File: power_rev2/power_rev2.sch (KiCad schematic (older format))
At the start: 74 parts, among them J1 Conn_01x02_Female, J2 Conn_01x02_Female, J3 CONN_02X03, J4 Conn_01x06_Female, Q1 BS170, Q11 BS170, Q12 BSB014N04LX3, Q2 BS170, Q3 BS170, Q5 BS170, Q6 BS170, Q7 BS170, U1 MAX1648, U2 TPS2592xx

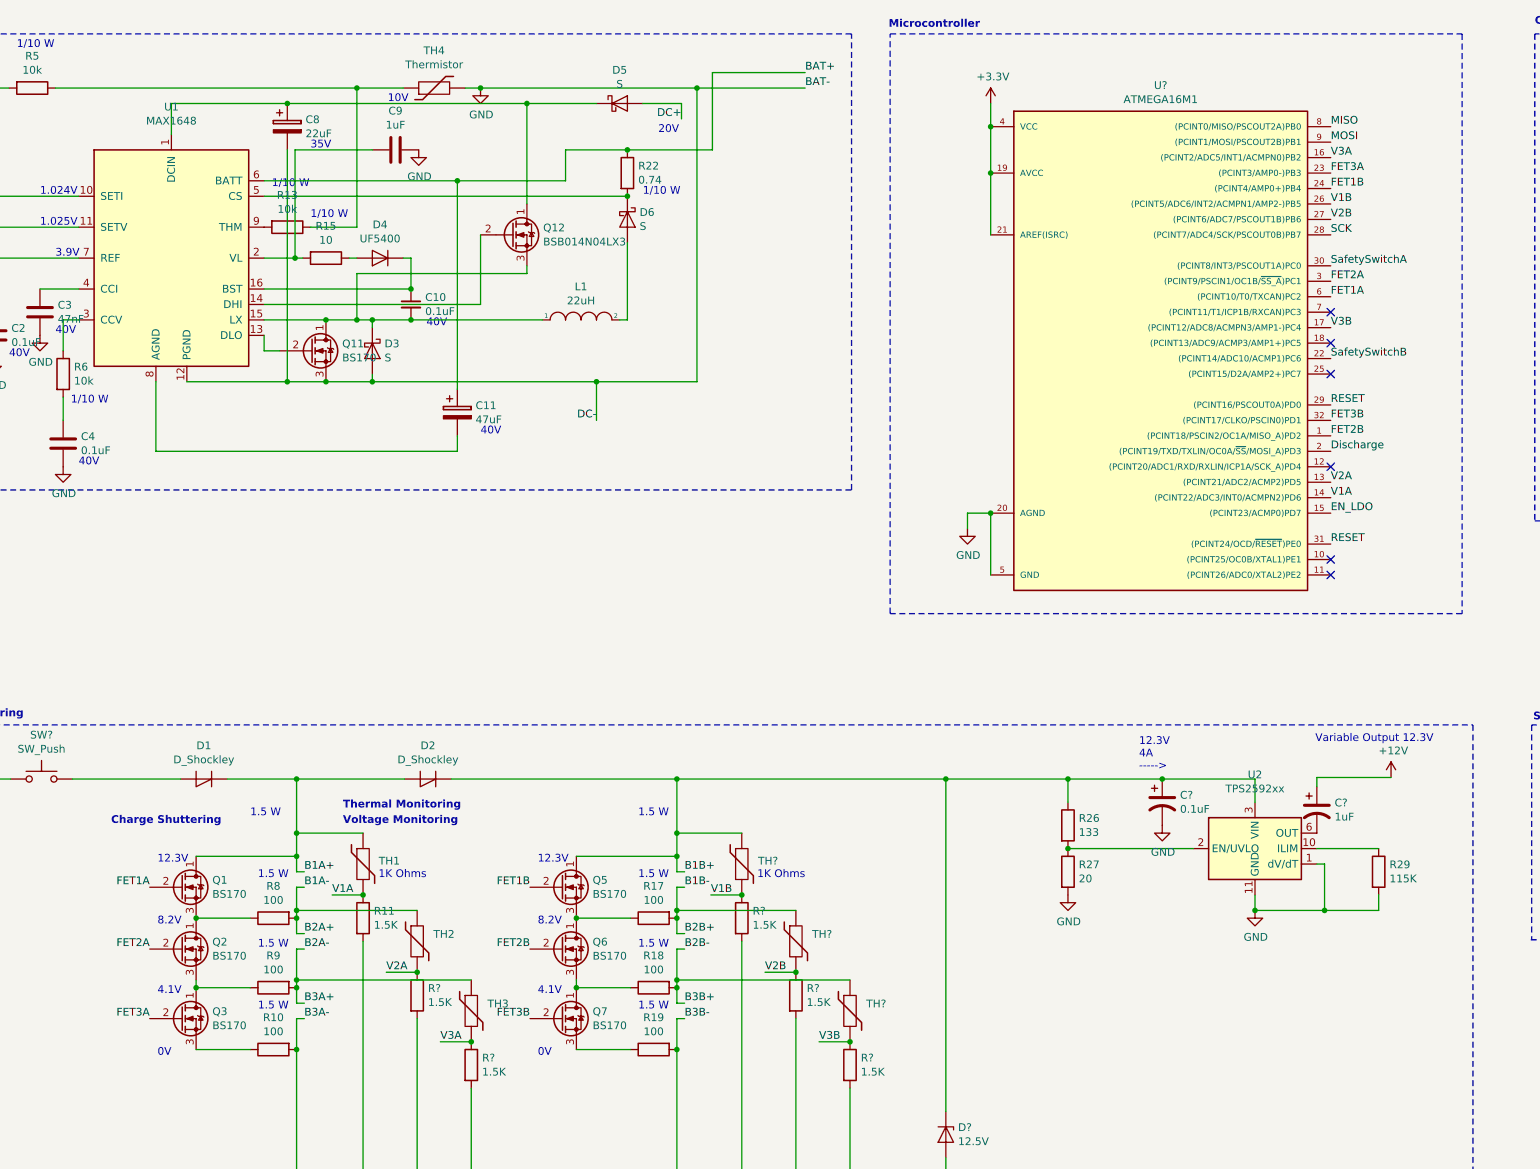
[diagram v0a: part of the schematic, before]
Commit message: balancing with bq rev 2
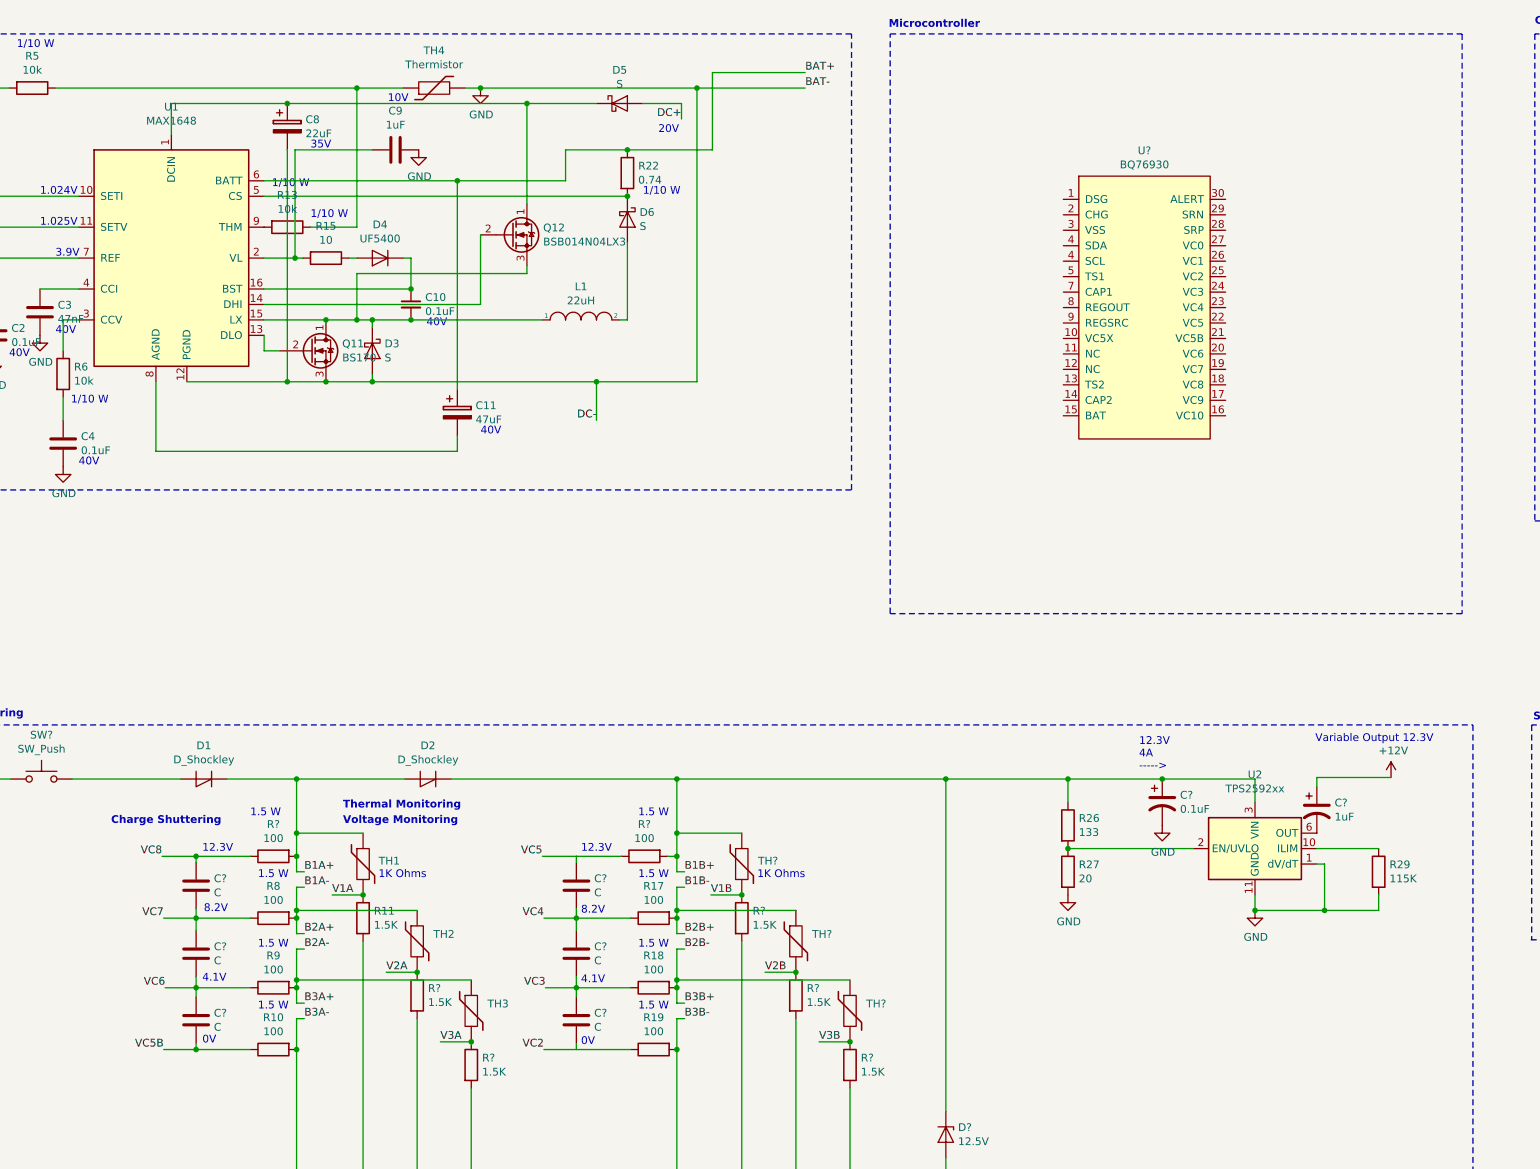
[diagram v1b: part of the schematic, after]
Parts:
- removed Q1, Q2, Q3, Q5, Q6, Q7: BS170, Package_TO_SOT_THT:TO-92_Inline, symbol Transistor_FET:BS170
- removed U?: ATMEGA16M1, footprints:TQFP-32_7x7mm_Pitch0.8mm, symbol formula:ATMEGA16M1
- added C? (x6): C, symbol Device:C
- added R? (x2): 100, Resistor_SMD:R_0805_2012Metric_Pad1.15x1.40mm_HandSolder, symbol Device:R
- added U?: BQ76930, symbol formula:BQ76930
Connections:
- net B1A+: now also R?.2
- net B1B+: now also R?.2
- net VC7: now reaches R8.1
- net VC7: now also C?.1, C?.2
- net VC6: now reaches R9.1
- net VC6: now also C?.1, C?.2
- net VC5B: now reaches R10.1
- net VC5B: now also C?.2
- net VC4: now reaches R17.1
- net VC4: now also C?.1, C?.2
- net VC3: now reaches R18.1
- net VC3: now also C?.1, C?.2
- net VC2: now reaches R19.1
- net VC2: now also C?.2
- new net VC5: C?.1, R?.1
- new net VC8: C?.1, R?.1
- no-connect marks 6 -> 0

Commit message: rev1 layout organization
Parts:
- added C? (x2): 1uF, symbol Device:C
- added D?: DIODE, symbol pspice:DIODE
- added R?: 10K, symbol Device:R
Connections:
- net GND: now also U?.3 (VSS), C?.1
- net VC2: now also U?.25 (VC2)
- net VC3: now also U?.24 (VC3)
- net VC4: now also U?.23 (VC4)
- net VC5: now also U?.22 (VC5), D?.1 (K)
- net VC5B: now also U?.21 (VC5B)
- net VC6: now also U?.20 (VC6)
- net VC7: now also U?.19 (VC7)
- net VC8: now also U?.18 (VC8)
- net at U?.10 (VC5X): now also C?.2, R?.1
- net at U?.13 (TS2): now also R?.2
- net at U?.14 (CAP2): now also C?.1
- net at U?.15 (BAT): now also D?.2 (A)
- net at U?.7 (CAP1): now also C?.2
- no-connect marks 0 -> 2
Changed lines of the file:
@@
 Connections
 Wire Notes Line
-	10730 4550 7030 4550
-Wire Notes Line
-	7030 4550 7030 800
+	10730 3750 7030 3750
+Wire Notes Line
+	7030 3750 7030 0
 Wire Notes Line
 	7030 800  10730 800
@@
 Variable Output 12.3V
 Wire Notes Line
-	10730 800  10730 4550
+	10730 20   10730 3770
 Wire Notes Line
 	550  5270 9600 5270
@@
 Text Label 4790 7370 2    50   ~ 0
 VC2
+Text Label 9200 3070 0    50   ~ 0
+VC8
+Text Label 9200 2970 0    50   ~ 0
+VC7
+Text Label 9200 2870 0    50   ~ 0
+VC6
+Text Label 9200 2770 0    50   ~ 0
+VC5B
+Text Label 9200 2570 0    50   ~ 0
+VC4
+Text Label 9200 2470 0    50   ~ 0
+VC3
+Text Label 9200 2370 0    50   ~ 0
+VC2
+Text Label 9200 2670 0    50   ~ 0
+VC5
+Wire Wire Line
+	8150 3070 7830 3070
+$Comp
+L Device:R R?
+U 1 1 5FF0B268
+P 7830 2920
+F 0 "R?" H 7900 2966 50  0000 L CNN
+F 1 "10K" H 7900 2875 50  0000 L CNN
+F 2 "" V 7760 2920 50  0001 C CNN
+F 3 "~" H 7830 2920 50  0001 C CNN
+	1    7830 2920
+	1    0    0    -1
+$EndComp
+Wire Wire Line
+	8150 2770 7830 2770
+NoConn ~ 8150 2870
+NoConn ~ 8150 2970
+$Comp
+L Device:C C?
+U 1 1 5FF2CD61
+P 7610 3020
+F 0 "C?" H 7495 2974 50  0000 R CNN
+F 1 "1uF" H 7495 3065 50  0000 R CNN
+F 2 "" H 7648 2870 50  0001 C CNN
+F 3 "~" H 7610 3020 50  0001 C CNN
+	1    7610 3020
+	-1   0    0    1
+$EndComp
+Wire Wire Line
+	8150 3170 7610 3170
+Wire Wire Line
+	7830 2770 7610 2770
+Wire Wire Line
+	7610 2770 7610 2870
+Connection ~ 7830 2770
+$Comp
+L pspice:DIODE D?
+U 1 1 5FF5ADE5
+P 8150 3470
+F 0 "D?" V 8196 3342 50  0000 R CNN
+F 1 "DIODE" V 8105 3342 50  0000 R CNN
+F 2 "" H 8150 3470 50  0001 C CNN
+F 3 "~" H 8150 3470 50  0001 C CNN
+	1    8150 3470
+	0    -1   -1   0
+$EndComp
+Text Label 8150 3670 3    50   ~ 0
+VC5
+$Comp
+L power:GND #PWR?
+U 1 1 5FF5C48B
+P 7630 2070
+F 0 "#PWR?" H 7630 1820 50  0001 C CNN
+F 1 "GND" H 7635 1897 50  0000 C CNN
+F 2 "" H 7630 2070 50  0001 C CNN
+F 3 "" H 7630 2070 50  0001 C CNN
+	1    7630 2070
+	1    0    0    -1
+$EndComp
+Wire Wire Line
+	8150 2070 7630 2070
+$Comp
+L Device:C C?
+U 1 1 5FF6830D
+P 7360 2620
+F 0 "C?" H 7245 2574 50  0000 R CNN
+F 1 "1uF" H 7245 2665 50  0000 R CNN
+F 2 "" H 7398 2470 50  0001 C CNN
+F 3 "~" H 7360 2620 50  0001 C CNN
+	1    7360 2620
+	-1   0    0    1
+$EndComp
+Wire Wire Line
+	8150 2470 7360 2470
+$Comp
+L power:GND #PWR?
+U 1 1 5FF74612
+P 7360 2770
+F 0 "#PWR?" H 7360 2520 50  0001 C CNN
+F 1 "GND" H 7365 2597 50  0000 C CNN
+F 2 "" H 7360 2770 50  0001 C CNN
+F 3 "" H 7360 2770 50  0001 C CNN
+	1    7360 2770
+	1    0    0    -1
+$EndComp
 $EndSCHEMATC
